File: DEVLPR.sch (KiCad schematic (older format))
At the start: 9 parts, among them CON1 SJ-3523-SMT-TR, P1 Power, P2 Analog, P3 Digital, P4 Digital, P5 CONN_01X01, P6 CONN_01X01, P7 CONN_01X01, P8 CONN_01X01

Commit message: Finalized rev dev.a.2 with improved filtering, power supply design, and silkscreen
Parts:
- added J1: EMG OUTPUT, digikey-footprints:PinHeader_6x2_P2.54mm_Horizontal, symbol dk_Rectangular-Connectors-Headers-Male-Pins:67996-412HLF
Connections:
- net labels added: EMG_OUT
- wire segments 50 -> 64
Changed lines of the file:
@@
 Wire Notes Line
 	10700 1000 10700 500
-$Sheet
-S 1500 3450 1750 1050
-U 6043E029
-F0 "EMG Amplifiers" 50
-F1 "emg_amplifier.sch" 50
-F2 "PASSIVE_LP_OUT" O R 3250 3750 50
-F3 "PASSIVE_HP_OUT" O R 3250 3850 50
-F4 "ACTIVE_HP_OUT" O R 3250 3950 50
-F5 "ACTIVE_LP_OUT" O R 3250 4050 50
-F6 "RAW_EMG" O R 3250 4150 50
-F7 "EMG_OUT" O R 3250 3650 50
-F8 "EMG_P" I L 1500 3600 50
-F9 "EMG_N" I L 1500 3700 50
-F10 "EMG_GND" I L 1500 3800 50
-$EndSheet
 $Comp
 L dk_Barrel-Audio-Connectors:SJ-3523-SMT-TR CON1
@@
 EMG_GND
 Wire Wire Line
-	1500 3600 950  3600
-Wire Wire Line
-	1500 3700 950  3700
-Wire Wire Line
-	1500 3800 950  3800
-Text Label 950  3600 0    50   ~ 0
+	1275 2050 725  2050
+Wire Wire Line
+	1275 2150 725  2150
+Wire Wire Line
+	1275 2250 725  2250
+Text Label 725  2050 0    50   ~ 0
 EMG_P
-Text Label 950  3700 0    50   ~ 0
+Text Label 725  2150 0    50   ~ 0
 EMG_N
-Text Label 950  3800 0    50   ~ 0
+Text Label 725  2250 0    50   ~ 0
 EMG_GND
-Wire Wire Line
-	3250 3650 3650 3650
-Wire Wire Line
-	3250 3750 3650 3750
-Wire Wire Line
-	3250 3850 3650 3850
-Wire Wire Line
-	3250 3950 3650 3950
-Wire Wire Line
-	3250 4050 3650 4050
-Wire Wire Line
-	3250 4150 3650 4150
-Text Label 3650 3650 2    50   ~ 0
-A0
-Text Label 3650 3750 2    50   ~ 0
-A1
-Text Label 3650 3850 2    50   ~ 0
-A2
-Text Label 3650 3950 2    50   ~ 0
-A3
-Text Label 3650 4050 2    60   ~ 0
-A4(SDA)
-Text Label 3650 4150 2    60   ~ 0
-A5(SCL)
 $Sheet
-S 4400 3400 1300 1200
+S 1275 3450 1300 1200
 U 605EF1AE
 F0 "-5V Source" 50
@@
 EndData
 $EndBitmap
+$Comp
+L dk_Rectangular-Connectors-Headers-Male-Pins:67996-412HLF J1
+U 1 1 60748A64
+P 7450 2700
+F 0 "J1" H 7450 3147 60  0000 C CNN
+F 1 "EMG OUTPUT" H 7450 3041 60  0000 C CNN
+F 2 "digikey-footprints:PinHeader_6x2_P2.54mm_Horizontal" H 7650 2900 60  0001 L CNN
+F 3 "https://cdn.amphenol-icc.com/media/wysiwyg/files/drawing/67996.pdf" H 7650 3000 60  0001 L CNN
+F 4 "609-3219-ND" H 7650 3100 60  0001 L CNN "Digi-Key_PN"
+F 5 "67996-412HLF" H 7650 3200 60  0001 L CNN "MPN"
+F 6 "Connectors, Interconnects" H 7650 3300 60  0001 L CNN "Category"
+F 7 "Rectangular Connectors - Headers, Male Pins" H 7650 3400 60  0001 L CNN "Family"
+F 8 "https://cdn.amphenol-icc.com/media/wysiwyg/files/drawing/67996.pdf" H 7650 3500 60  0001 L CNN "DK_Datasheet_Link"
+F 9 "/product-detail/en/amphenol-icc-fci/67996-412HLF/609-3219-ND/1878508" H 7650 3600 60  0001 L CNN "DK_Detail_Page"
+F 10 "CONN HEADER VERT 12POS 2.54MM" H 7650 3700 60  0001 L CNN "Description"
+F 11 "Amphenol ICC (FCI)" H 7650 3800 60  0001 L CNN "Manufacturer"
+F 12 "Active" H 7650 3900 60  0001 L CNN "Status"
+	1    7450 2700
+	1    0    0    -1
+$EndComp
+Wire Wire Line
+	7250 2500 7150 2500
+Wire Wire Line
+	7150 2500 7150 2600
+Wire Wire Line
+	7150 3000 7250 3000
+Wire Wire Line
+	7250 2900 7150 2900
+Connection ~ 7150 2900
+Wire Wire Line
+	7150 2900 7150 3000
+Wire Wire Line
+	7250 2800 7150 2800
+Connection ~ 7150 2800
+Wire Wire Line
+	7150 2800 7150 2900
+Wire Wire Line
+	7250 2700 7150 2700
+Connection ~ 7150 2700
+Wire Wire Line
+	7150 2700 7150 2750
+Wire Wire Line
+	7250 2600 7150 2600
+Connection ~ 7150 2600
+Wire Wire Line
+	7150 2600 7150 2700
+Connection ~ 7150 2750
+Wire Wire Line
+	7150 2750 7150 2800
+Text Label 8075 3000 2    60   ~ 0
+A0
+Text Label 8075 2900 2    60   ~ 0
+A1
+Text Label 8075 2800 2    60   ~ 0
+A2
+Text Label 8075 2700 2    60   ~ 0
+A3
+Text Label 8075 2600 2    60   ~ 0
+A4(SDA)
+Wire Wire Line
+	7650 2900 8075 2900
+Wire Wire Line
+	7650 3000 8075 3000
+Text Label 8075 2500 2    60   ~ 0
+A5(SCL)
+Wire Wire Line
+	7650 2800 8075 2800
+Wire Wire Line
+	7650 2500 8075 2500
+Wire Wire Line
+	7650 2600 8075 2600
+Wire Wire Line
+	7650 2700 8075 2700
+$Sheet
+S 1275 1900 1750 1050
+U 6043E029
+F0 "EMG Amplifiers" 50
+F1 "emg_amplifier.sch" 50
+F2 "EMG_OUT" O R 3025 2100 50
+F3 "EMG_P" I L 1275 2050 50
+F4 "EMG_N" I L 1275 2150 50
+F5 "EMG_GND" I L 1275 2250 50
+$EndSheet
+Text Label 3425 2100 2    50   ~ 0
+EMG_OUT
+Wire Wire Line
+	3025 2100 3425 2100
+Text Label 6675 2750 0    50   ~ 0
+EMG_OUT
+Wire Wire Line
+	6675 2750 7150 2750
 $EndSCHEMATC

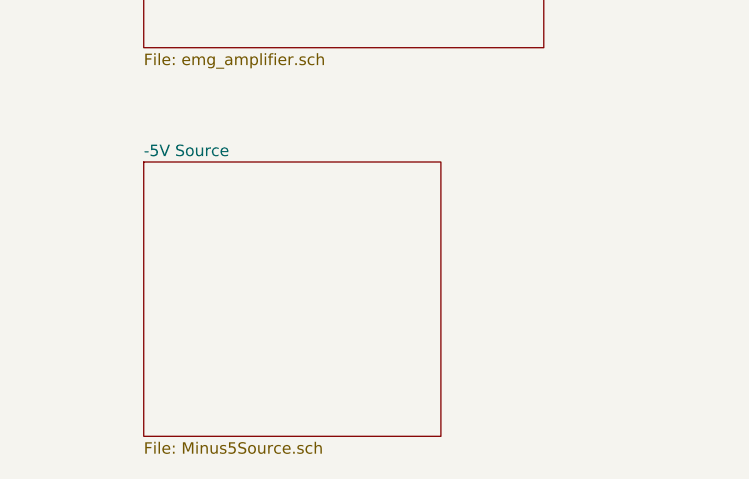
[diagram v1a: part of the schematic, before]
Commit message: Major overhaul given chip shortage. Completely redid the power supply, and refined the amps for the EMG to give better gain and use the full output range
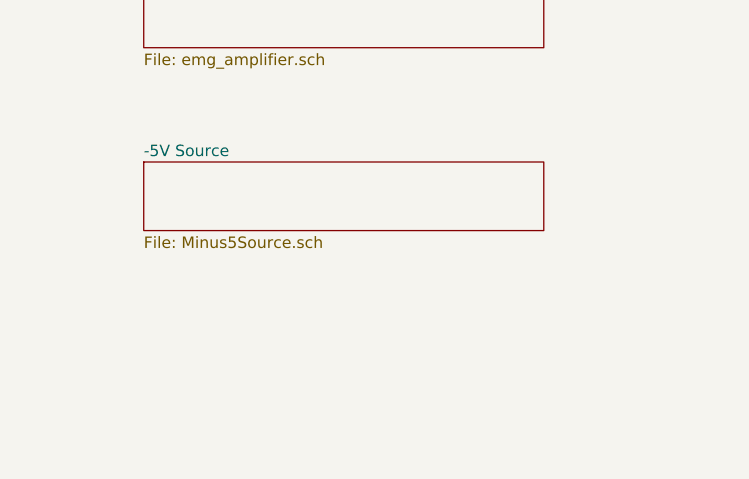
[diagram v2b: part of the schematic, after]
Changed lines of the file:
@@
 EMG_GND
 $Sheet
-S 1275 3450 1300 1200
+S 1275 3450 1750 300
 U 605EF1AE
 F0 "-5V Source" 50

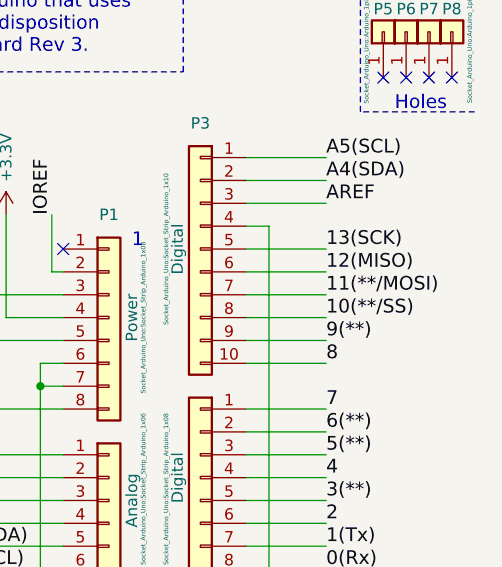
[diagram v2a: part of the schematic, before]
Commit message: Fixed SPI signal naming convention to new OSHWA proposal
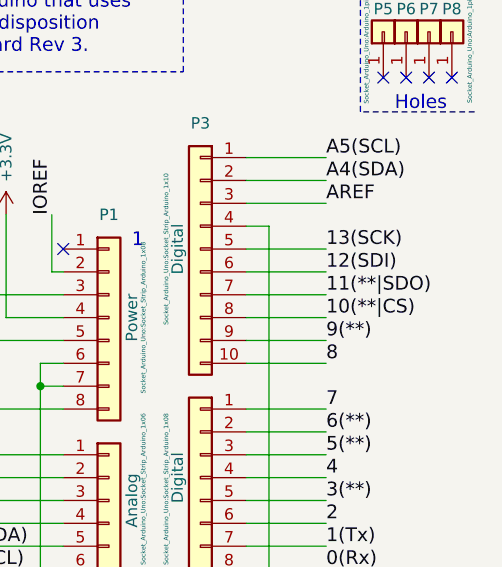
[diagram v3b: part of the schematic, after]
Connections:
- net labels added: 10(**|CS), 11(**|SDO), 12(SDI)
- net labels removed: 10(**/SS), 11(**/MOSI), 12(MISO)
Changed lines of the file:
@@
 9(**)
 Text Label 10550 1900 0    60   ~ 0
-10(**/SS)
+10(**|CS)
 Text Label 10550 1800 0    60   ~ 0
-11(**/MOSI)
+11(**|SDO)
 Text Label 10550 1700 0    60   ~ 0
-12(MISO)
+12(SDI)
 Text Label 10550 1600 0    60   ~ 0
 13(SCK)

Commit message: Finished rev dev.a.4 with safety improvements, better gain settings, and dc offset removal
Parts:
- added TP1: EMG_N, digikey-footprints:Test_Point_D1.02mm, symbol dk_Test-Points:5011
- added TP2: EMG_P, digikey-footprints:Test_Point_D1.02mm, symbol dk_Test-Points:5011
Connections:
- net labels added: SCL, SDA
- wire segments 64 -> 68
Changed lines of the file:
@@
 NoConn ~ 9400 1600
 Text Label 10550 1300 0    60   ~ 0
-A4(SDA)
+SDA
 Text Label 10550 1200 0    60   ~ 0
-A5(SCL)
+SCL
 Text Notes 10850 1000 0    60   ~ 0
 Holes
@@
 $EndComp
 Wire Wire Line
-	1550 1000 1850 1000
-Wire Wire Line
-	1550 1100 1850 1100
-Wire Wire Line
 	1550 1200 1850 1200
-Text Label 1850 1100 2    50   ~ 0
+Text Label 2275 1100 2    50   ~ 0
 EMG_P
-Text Label 1850 1000 2    50   ~ 0
+Text Label 2275 1000 2    50   ~ 0
 EMG_N
 Text Label 1850 1200 2    50   ~ 0
@@
 Wire Wire Line
 	6675 2750 7150 2750
+$Comp
+L dk_Test-Points:5011 TP2
+U 1 1 60A0F888
+P 1950 1275
+AR Path="/60A0F888" Ref="TP2"  Part="1"
+AR Path="/605EF1AE/60A0F888" Ref="TP?"  Part="1"
+F 0 "TP2" H 1900 1322 50  0001 R CNN
+F 1 "EMG_P" H 2075 1200 50  0000 R CNN
+F 2 "digikey-footprints:Test_Point_D1.02mm" H 2150 1475 60  0001 L CNN
+F 3 "http://www.keyelco.com/product-pdf.cfm?p=1320" H 2150 1575 60  0001 L CNN
+F 4 "36-5011-ND" H 2150 1675 60  0001 L CNN "Digi-Key_PN"
+F 5 "5011" H 2150 1775 60  0001 L CNN "MPN"
+F 6 "Test and Measurement" H 2150 1875 60  0001 L CNN "Category"
+F 7 "Test Points" H 2150 1975 60  0001 L CNN "Family"
+F 8 "http://www.keyelco.com/product-pdf.cfm?p=1320" H 2150 2075 60  0001 L CNN "DK_Datasheet_Link"
+F 9 "/product-detail/en/keystone-electronics/5011/36-5011-ND/255333" H 2150 2175 60  0001 L CNN "DK_Detail_Page"
+F 10 "PC TEST POINT MULTIPURPOSE BLACK" H 2150 2275 60  0001 L CNN "Description"
+F 11 "Keystone Electronics" H 2150 2375 60  0001 L CNN "Manufacturer"
+F 12 "Active" H 2150 2475 60  0001 L CNN "Status"
+	1    1950 1275
+	1    0    0    -1
+$EndComp
+$Comp
+L dk_Test-Points:5011 TP1
+U 1 1 60A17C25
+P 1950 825
+AR Path="/60A17C25" Ref="TP1"  Part="1"
+AR Path="/605EF1AE/60A17C25" Ref="TP?"  Part="1"
+F 0 "TP1" H 1900 872 50  0001 R CNN
+F 1 "EMG_N" H 2075 750 50  0000 R CNN
+F 2 "digikey-footprints:Test_Point_D1.02mm" H 2150 1025 60  0001 L CNN
+F 3 "http://www.keyelco.com/product-pdf.cfm?p=1320" H 2150 1125 60  0001 L CNN
+F 4 "36-5011-ND" H 2150 1225 60  0001 L CNN "Digi-Key_PN"
+F 5 "5011" H 2150 1325 60  0001 L CNN "MPN"
+F 6 "Test and Measurement" H 2150 1425 60  0001 L CNN "Category"
+F 7 "Test Points" H 2150 1525 60  0001 L CNN "Family"
+F 8 "http://www.keyelco.com/product-pdf.cfm?p=1320" H 2150 1625 60  0001 L CNN "DK_Datasheet_Link"
+F 9 "/product-detail/en/keystone-electronics/5011/36-5011-ND/255333" H 2150 1725 60  0001 L CNN "DK_Detail_Page"
+F 10 "PC TEST POINT MULTIPURPOSE BLACK" H 2150 1825 60  0001 L CNN "Description"
+F 11 "Keystone Electronics" H 2150 1925 60  0001 L CNN "Manufacturer"
+F 12 "Active" H 2150 2025 60  0001 L CNN "Status"
+	1    1950 825
+	-1   0    0    1
+$EndComp
+Wire Wire Line
+	1550 1100 1950 1100
+Wire Wire Line
+	1550 1000 1950 1000
+Wire Wire Line
+	1950 925  1950 1000
+Connection ~ 1950 1000
+Wire Wire Line
+	1950 1000 2275 1000
+Wire Wire Line
+	1950 1175 1950 1100
+Connection ~ 1950 1100
+Wire Wire Line
+	1950 1100 2275 1100
 $EndSCHEMATC
